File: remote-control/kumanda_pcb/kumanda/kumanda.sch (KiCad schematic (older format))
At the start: 24 parts, among them J1 USB_A, J2 Conn_01x04, J3 RJ45, U1 MEGA_PRO_EMBED_CH340G___ATMEG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

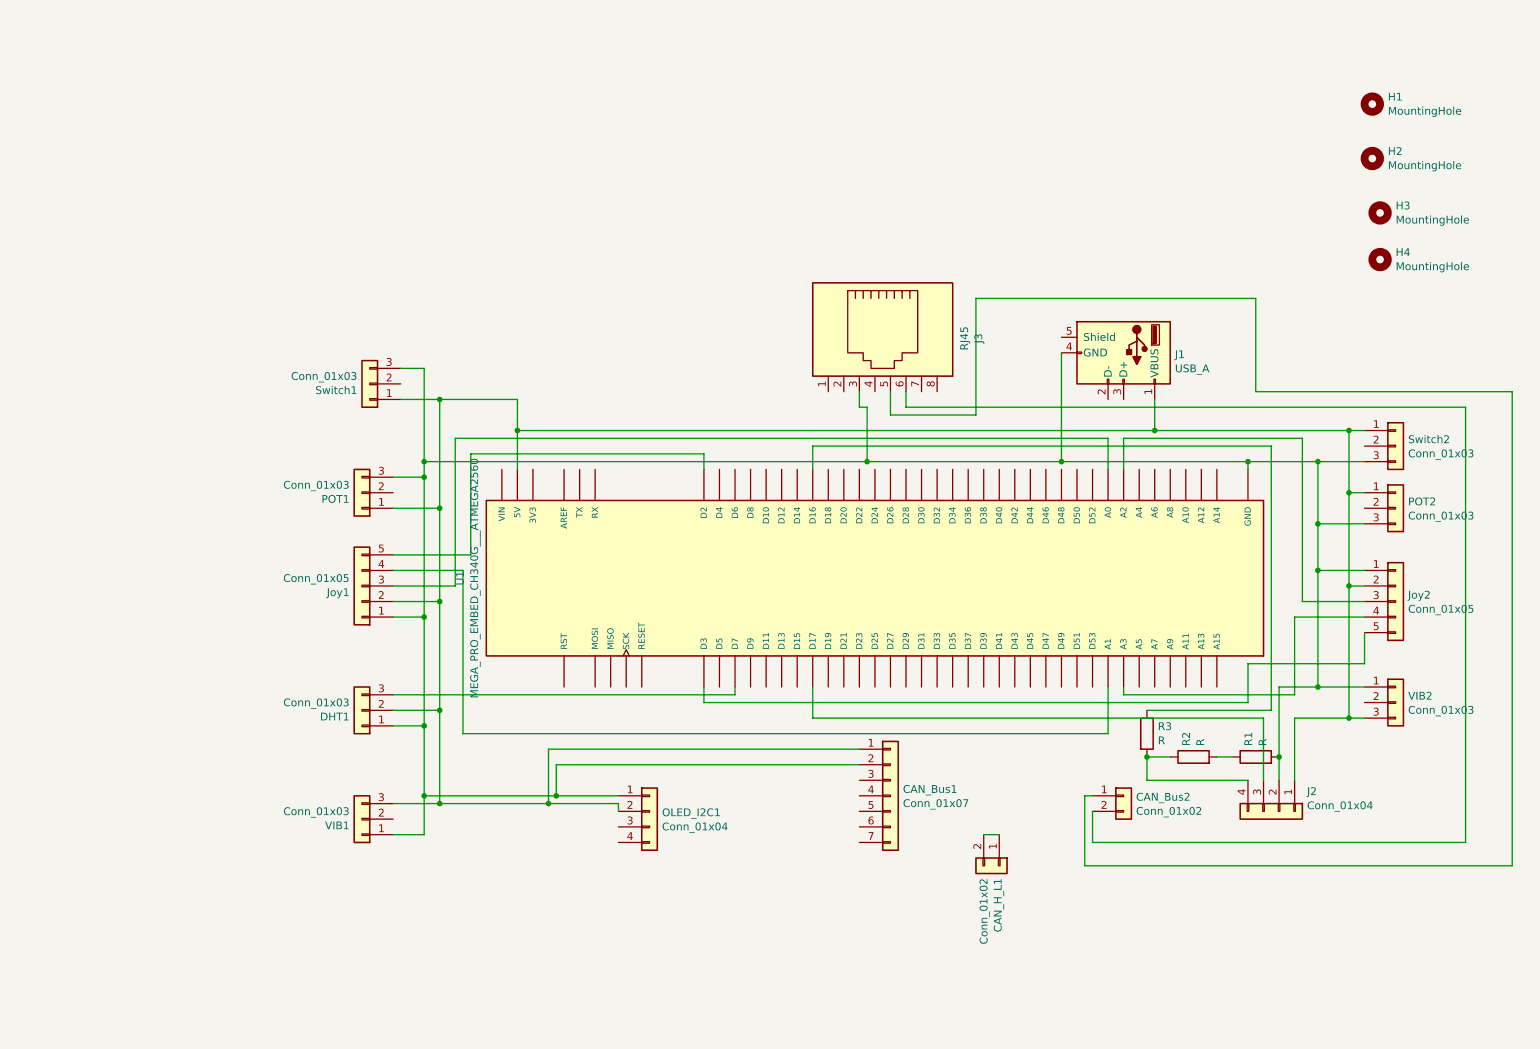
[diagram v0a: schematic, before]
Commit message: Schematic updated, free pins and av conventer not added
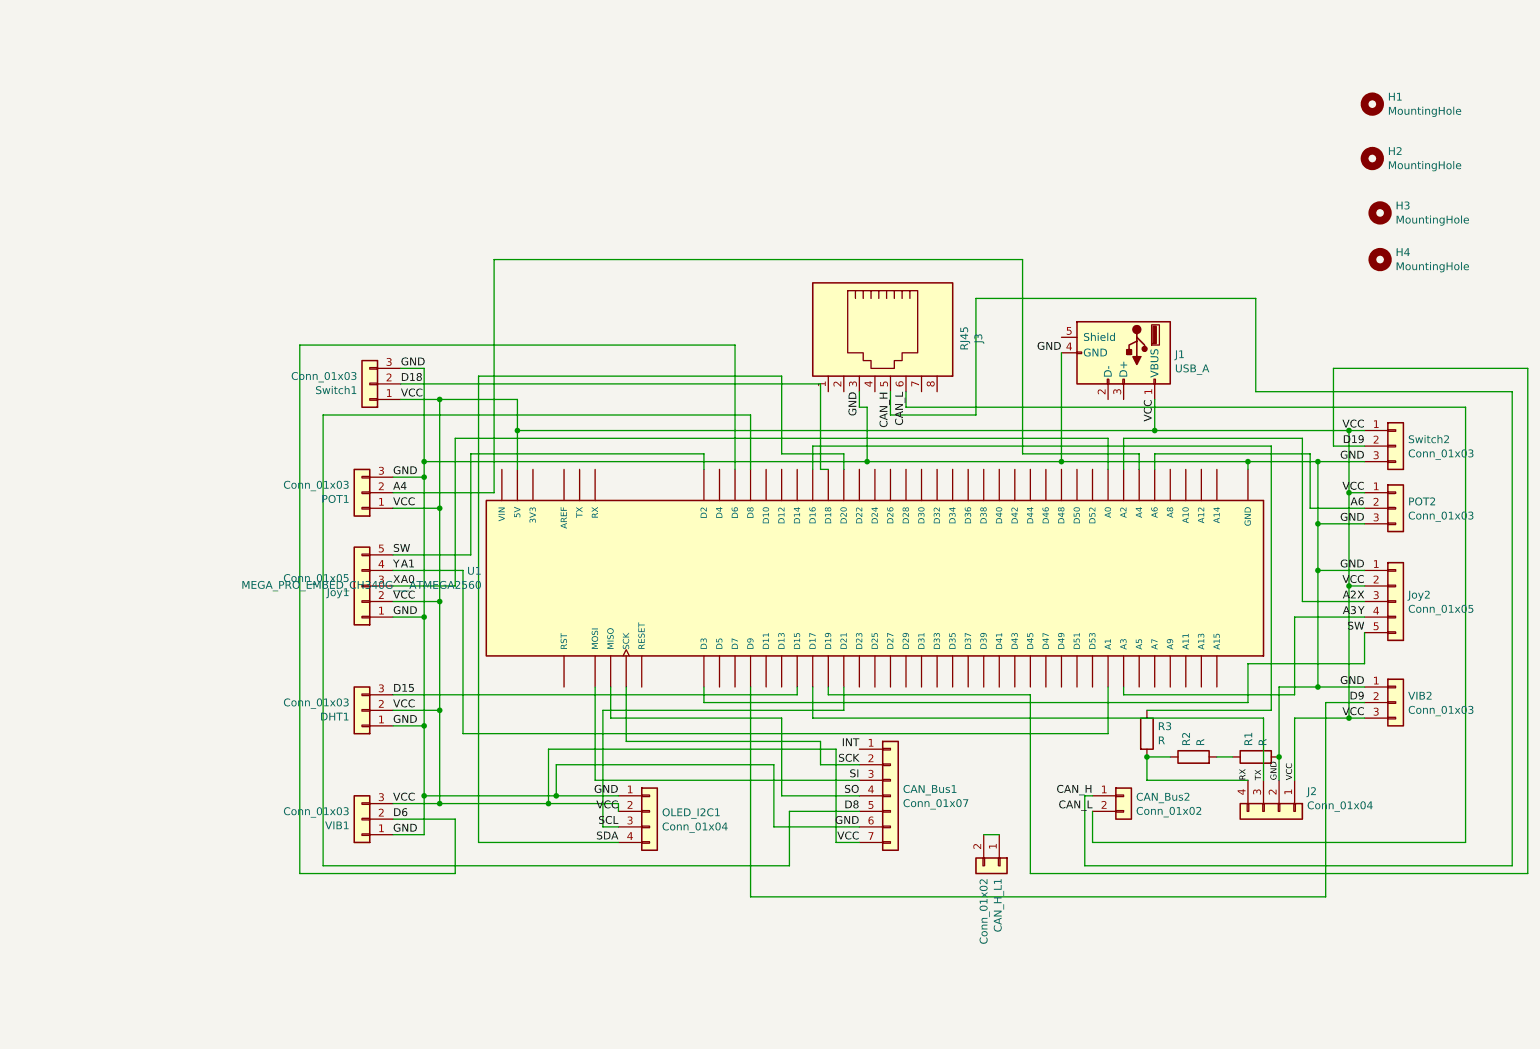
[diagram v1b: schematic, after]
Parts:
- removed U1: MEGA_PRO_EMBED_CH340G___ATMEGA2560, MODULE_MEGA_PRO_EMBED_CH340G_:_ATMEGA2560, symbol MEGA_PRO_EMBED_CH340G___ATMEGA2560:MEGA_PRO_EMBED_CH340G___ATMEGA2560
- added U1: MEGA_PRO_EMBED_CH340G___ATMEGA2560, MODULE_MEGA_PRO_EMBED_CH340G_git:_ATMEGA2560, symbol MEGA_PRO_EMBED_CH340G___ATMEGA2560-git:MEGA_PRO_EMBED_CH340G___ATMEGA2560
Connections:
- net VCC: now reaches DHT1.2 (Pin_2), J1.1 (VBUS), J2.1 (Pin_1), Joy1.2 (Pin_2), Joy2.2 (Pin_2), OLED_I2C1.2 (Pin_2), POT1.1 (Pin_1), POT2.1 (Pin_1), Switch1.1 (Pin_1), Switch2.1 (Pin_1), VIB1.3 (Pin_3), VIB2.3 (Pin_3)
- net VCC: now also CAN_Bus1.7 (Pin_7), U1.5V_1 (5V), U1.5V_2 (5V), U1.5V_3 (5V); no longer CAN_Bus1.1 (Pin_1)
- net A0: now reaches Joy1.3 (Pin_3)
- net A0: now also Joy2.3 (Pin_3), U1.A0, U1.A2
- net A1: now reaches Joy1.4 (Pin_4)
- net A1: now also Joy2.4 (Pin_4), U1.A1, U1.A3
- net at R3.1: now also U1.D16
- net TX: now reaches J2.3 (Pin_3)
- net TX: now also U1.D17
- net SW: now reaches Joy1.5 (Pin_5)
- net SW: now also Joy2.5 (Pin_5), U1.D2, U1.D3
- net D15: now reaches DHT1.3 (Pin_3)
- net D15: now also U1.D15
- net GND: now reaches DHT1.1 (Pin_1), J1.4 (GND), J2.2 (Pin_2), J3.3, Joy1.1 (Pin_1), Joy2.1 (Pin_1), OLED_I2C1.1 (Pin_1), POT1.3 (Pin_3), POT2.3 (Pin_3), R1.2, Switch1.3 (Pin_3), Switch2.3 (Pin_3), VIB1.1 (Pin_1), VIB2.1 (Pin_1)
- net GND: now also CAN_Bus1.6 (Pin_6), U1.GND_1 (GND), U1.GND_2 (GND), U1.GND_3 (GND); no longer CAN_Bus1.2 (Pin_2)
- net D6: now reaches VIB1.2 (Pin_2)
- net D6: now also U1.D6
- net A4: now reaches POT1.2 (Pin_2)
- net A4: now also U1.A4
- net A6: now reaches POT2.2 (Pin_2)
- net A6: now also U1.A6
- net SCL: now reaches OLED_I2C1.3 (Pin_3)
- net SCL: now also U1.D21
- net SDA: now reaches OLED_I2C1.4 (Pin_4)
- net SDA: now also U1.D20
- net D9: now reaches VIB2.2 (Pin_2)
- net D9: now also U1.D9
- net SI: now reaches CAN_Bus1.3 (Pin_3)
- net SI: now also U1.MOSI
- net SO: now reaches CAN_Bus1.4 (Pin_4)
- net SO: now also U1.MISO
- net D8: now reaches CAN_Bus1.5 (Pin_5)
- net D8: now also U1.D8
- net CAN_H: now reaches CAN_Bus2.1 (Pin_1), J3.5
- net CAN_L: now reaches CAN_Bus2.2 (Pin_2), J3.6
- net D18: now reaches Switch1.2 (Pin_2)
- net D18: now also U1.D18
- net D19: now reaches Switch2.2 (Pin_2)
- net D19: now also U1.D19
- net RX: now reaches J2.4 (Pin_4), R2.1, R3.2
- new net: U1.3V3_1 (3V3), U1.3V3_2 (3V3)
- new net: U1.VIN_1 (VIN), U1.VIN_2 (VIN)
- new net INT: CAN_Bus1.1 (Pin_1)
- new net SCK: CAN_Bus1.2 (Pin_2), U1.SCK

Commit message: Everything finished except footprints of screw terminal.
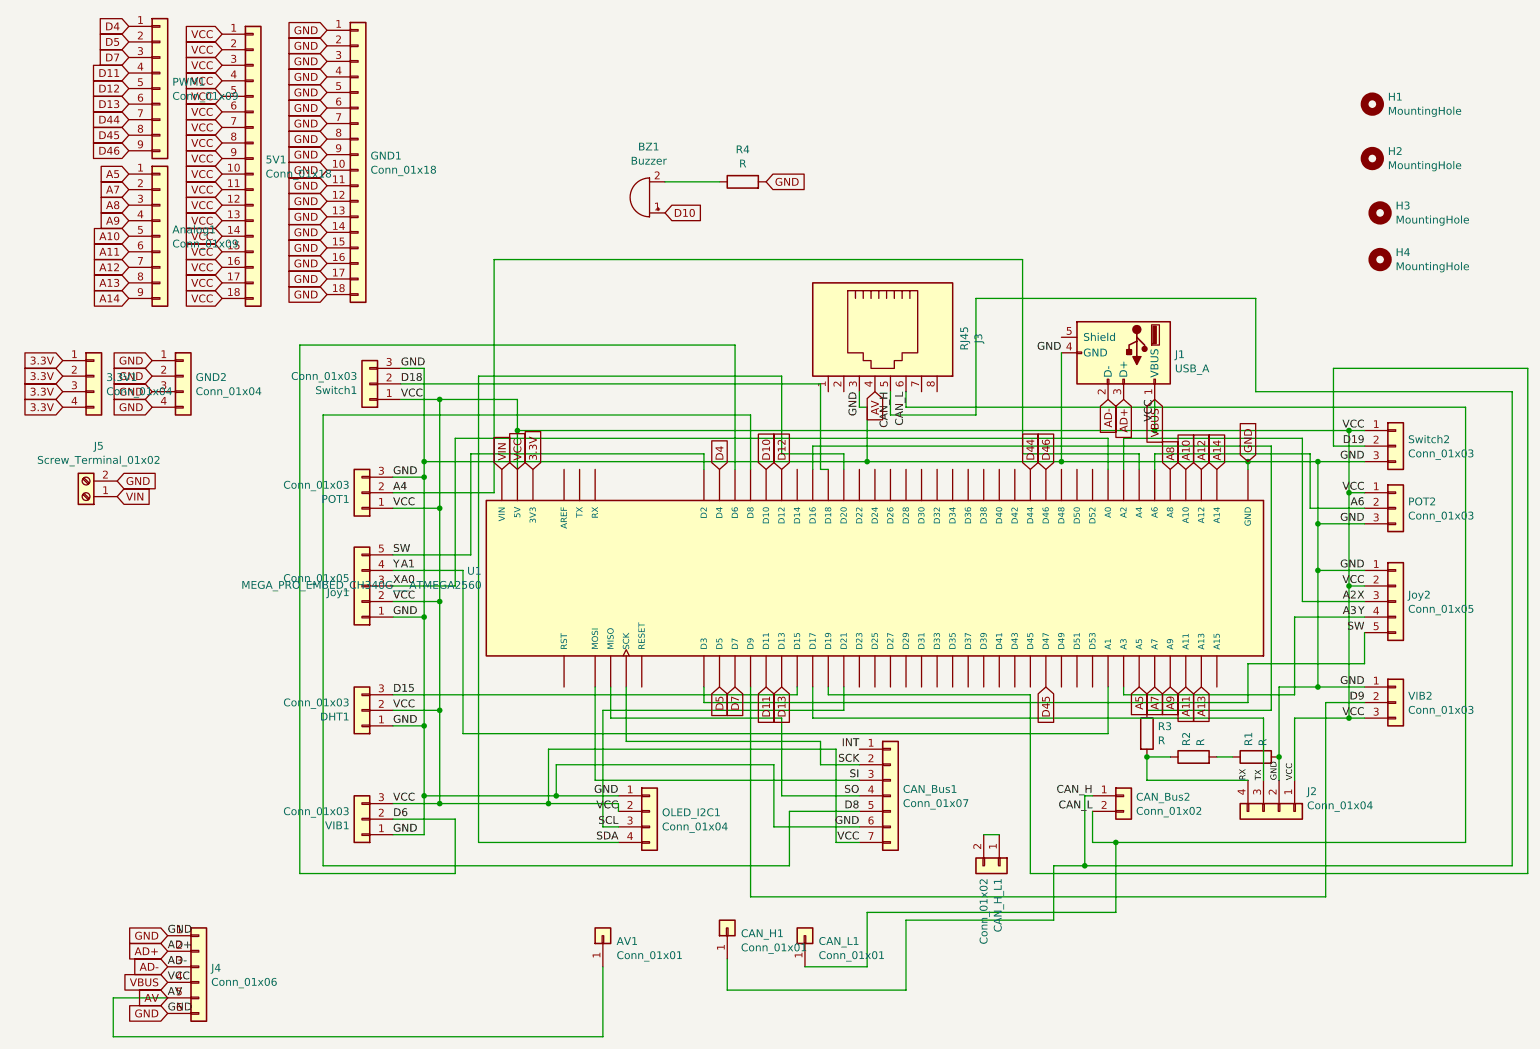
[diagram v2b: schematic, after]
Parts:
- added 3.3V1, GND2: Conn_01x04, Connector_PinHeader_2.54mm:PinHeader_1x04_P2.54mm_Vertical, symbol Connector_Generic:Conn_01x04
- added 5V1, GND1: Conn_01x18, Connector_PinHeader_2.54mm:PinHeader_1x18_P2.54mm_Vertical, symbol Connector_Generic:Conn_01x18
- added AV1, CAN_H1, CAN_L1: Conn_01x01, symbol Connector_Generic:Conn_01x01
- added Analog1, PWM1: Conn_01x09, Connector_PinHeader_2.54mm:PinHeader_1x09_P2.54mm_Vertical, symbol Connector_Generic:Conn_01x09
- added BZ1: Buzzer, Buzzer_Beeper:Buzzer_12x9.5RM7.6, symbol Device:Buzzer
- added J4: Conn_01x06, analog_cam:Analog-cam, symbol Connector_Generic:Conn_01x06
- added J5: Screw_Terminal_01x02, symbol Connector:Screw_Terminal_01x02
- added R4: R, Resistor_THT:R_Axial_DIN0207_L6.3mm_D2.5mm_P7.62mm_Horizontal, symbol Device:R
- CAN_Bus1: footprint Connector_Molex:Molex_KK-254_AE-6410-07A_1x07_P2.54mm_Vertical -> Connector_PinHeader_2.54mm:PinHeader_1x07_P2.54mm_Vertical
- CAN_Bus2, CAN_H_L1: footprint Connector_Molex:Molex_KK-254_AE-6410-02A_1x02_P2.54mm_Vertical -> Connector_PinHeader_2.54mm:PinHeader_1x02_P2.54mm_Vertical
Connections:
- net CAN_H: now also CAN_H1.1 (Pin_1)
- net CAN_L: now also CAN_L1.1 (Pin_1)
- net GND: now also GND1.1 (Pin_1), GND1.10 (Pin_10), GND1.11 (Pin_11), GND1.12 (Pin_12), GND1.13 (Pin_13), GND1.14 (Pin_14), GND1.15 (Pin_15), GND1.16 (Pin_16), GND1.17 (Pin_17), GND1.18 (Pin_18), GND1.2 (Pin_2), GND1.3 (Pin_3), GND1.4 (Pin_4), GND1.5 (Pin_5), GND1.6 (Pin_6), GND1.7 (Pin_7), GND1.8 (Pin_8), GND1.9 (Pin_9), GND2.1 (Pin_1), GND2.2 (Pin_2), GND2.3 (Pin_3), GND2.4 (Pin_4), J4.1 (Pin_1), J4.6 (Pin_6), J5.2 (Pin_2), R4.2
- net AV: now reaches J3.4
- net AV: now also AV1.1 (Pin_1), J4.5 (Pin_5)
- net 3.3V: now reaches U1.3V3_1 (3V3), U1.3V3_2 (3V3)
- net 3.3V: now also 3.3V1.1 (Pin_1), 3.3V1.2 (Pin_2), 3.3V1.3 (Pin_3), 3.3V1.4 (Pin_4)
- net A10: now reaches U1.A10
- net A10: now also Analog1.5 (Pin_5)
- net A11: now reaches U1.A11
- net A11: now also Analog1.6 (Pin_6)
- net A12: now reaches U1.A12
- net A12: now also Analog1.7 (Pin_7)
- net A13: now reaches U1.A13
- net A13: now also Analog1.8 (Pin_8)
- net A14: now reaches U1.A14
- net A14: now also Analog1.9 (Pin_9)
- net A5: now reaches U1.A5
- net A5: now also Analog1.1 (Pin_1)
- net A7: now reaches U1.A7
- net A7: now also Analog1.2 (Pin_2)
- net A8: now reaches U1.A8
- net A8: now also Analog1.3 (Pin_3)
- net A9: now reaches U1.A9
- net A9: now also Analog1.4 (Pin_4)
- net D10: now reaches U1.D10
- net D10: now also BZ1.1 (-)
- net D11: now reaches U1.D11
- net D11: now also PWM1.4 (Pin_4)
- net D12: now reaches U1.D12
- net D12: now also PWM1.5 (Pin_5)
- net D13: now reaches U1.D13
- net D13: now also PWM1.6 (Pin_6)
- net D4: now reaches U1.D4
- net D4: now also PWM1.1 (Pin_1)
- net D44: now reaches U1.D44
- net D44: now also PWM1.7 (Pin_7)
- net D46: now reaches U1.D46
- net D46: now also PWM1.9 (Pin_9)
- net D45: now reaches U1.D47
- net D45: now also PWM1.8 (Pin_8)
- net D5: now reaches U1.D5
- net D5: now also PWM1.2 (Pin_2)
- net D7: now reaches U1.D7
- net D7: now also PWM1.3 (Pin_3)
- net VIN: now reaches U1.VIN_1 (VIN), U1.VIN_2 (VIN)
- net VIN: now also J5.1 (Pin_1)
- net AD-: now reaches J1.2 (D-)
- net AD-: now also J4.3 (Pin_3)
- net AD+: now reaches J1.3 (D+)
- net AD+: now also J4.2 (Pin_2)
- net VCC renamed VBUS
- net VBUS: now also 5V1.1 (Pin_1), 5V1.10 (Pin_10), 5V1.11 (Pin_11), 5V1.12 (Pin_12), 5V1.13 (Pin_13), 5V1.14 (Pin_14), 5V1.15 (Pin_15), 5V1.16 (Pin_16), 5V1.17 (Pin_17), 5V1.18 (Pin_18), 5V1.2 (Pin_2), 5V1.3 (Pin_3), 5V1.4 (Pin_4), 5V1.5 (Pin_5), 5V1.6 (Pin_6), 5V1.7 (Pin_7), 5V1.8 (Pin_8), 5V1.9 (Pin_9), J4.4 (Pin_4)
- new net: BZ1.2 (+), R4.1

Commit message: Schematic finished
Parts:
- AV1, CAN_H1, CAN_L1: footprint (none) -> Connector_PinHeader_2.54mm:PinHeader_1x01_P2.54mm_Vertical
- J5: footprint (none) -> TerminalBlock_Phoenix:TerminalBlock_Phoenix_PT-1,5-2-3.5-H_1x02_P3.50mm_Horizontal
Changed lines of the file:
@@
 F 0 "AV1" V 4414 6512 50  0000 R CNN
 F 1 "Conn_01x01" V 4323 6512 50  0000 R CNN
-F 2 "" H 4450 6600 50  0001 C CNN
+F 2 "Connector_PinHeader_2.54mm:PinHeader_1x01_P2.54mm_Vertical" H 4450 6600 50  0001 C CNN
 F 3 "~" H 4450 6600 50  0001 C CNN
 	1    4450 6600
@@
 F 0 "CAN_L1" V 5714 6512 50  0000 R CNN
 F 1 "Conn_01x01" V 5623 6512 50  0000 R CNN
-F 2 "" H 5750 6600 50  0001 C CNN
+F 2 "Connector_PinHeader_2.54mm:PinHeader_1x01_P2.54mm_Vertical" H 5750 6600 50  0001 C CNN
 F 3 "~" H 5750 6600 50  0001 C CNN
 	1    5750 6600
@@
 F 0 "CAN_H1" V 5214 6462 50  0000 R CNN
 F 1 "Conn_01x01" V 5123 6462 50  0000 R CNN
-F 2 "" H 5250 6550 50  0001 C CNN
+F 2 "Connector_PinHeader_2.54mm:PinHeader_1x01_P2.54mm_Vertical" H 5250 6550 50  0001 C CNN
 F 3 "~" H 5250 6550 50  0001 C CNN
 	1    5250 6550
@@
 F 0 "J5" H 1043 3450 50  0000 C CNN
 F 1 "Screw_Terminal_01x02" H 1043 3541 50  0000 C CNN
-F 2 "" H 1125 3775 50  0001 C CNN
+F 2 "TerminalBlock_Phoenix:TerminalBlock_Phoenix_PT-1,5-2-3.5-H_1x02_P3.50mm_Horizontal" H 1125 3775 50  0001 C CNN
 F 3 "~" H 1125 3775 50  0001 C CNN
 	1    1125 3775

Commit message: Schematic finished.
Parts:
- added USB_kod1: Conn_01x06, Connector_PinHeader_2.54mm:PinHeader_1x06_P2.54mm_Vertical, symbol Connector_Generic:Conn_01x06
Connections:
- net GND: now also USB_kod1.4 (Pin_4)
- net RX: now also USB_kod1.2 (Pin_2)
- net TX: now also USB_kod1.3 (Pin_3)
- net DTR: now reaches U1.RESET
- net DTR: now also USB_kod1.6 (Pin_6)
- new net 5v: USB_kod1.5 (Pin_5)
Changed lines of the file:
@@
 Text GLabel 3800 3600 1    50   Input ~ 0
 VIN
+$Comp
+L Connector_Generic:Conn_01x06 USB_kod1
+U 1 1 60CFD659
+P 1325 5000
+F 0 "USB_kod1" H 1405 4992 50  0000 L CNN
+F 1 "Conn_01x06" H 1405 4901 50  0000 L CNN
+F 2 "Connector_PinHeader_2.54mm:PinHeader_1x06_P2.54mm_Vertical" H 1325 5000 50  0001 C CNN
+F 3 "~" H 1325 5000 50  0001 C CNN
+	1    1325 5000
+	1    0    0    -1
+$EndComp
+Text GLabel 1125 4900 0    50   Input ~ 0
+RX
+Text GLabel 1125 5000 0    50   Input ~ 0
+TX
+Text GLabel 1125 5100 0    50   Input ~ 0
+GND
+Text GLabel 1125 5200 0    50   Input ~ 0
+5v
+Text GLabel 1125 5300 0    50   Input ~ 0
+DTR
+Text GLabel 4700 5000 3    50   Input ~ 0
+DTR
 $EndSCHEMATC
